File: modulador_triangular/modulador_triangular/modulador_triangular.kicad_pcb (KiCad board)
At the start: 2 copper layers, 50 x 44.5 mm, 12 parts, among them J1 OUT, J2 V1_12, J3 SIN, U1_2 ADTL082, U3 LT1016, U4 ADTL082

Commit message: commit express
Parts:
- added U1: LM7806_TO220, Package_TO_SOT_THT:TO-220-3_Vertical, F.Cu at (157.2, 79.2)
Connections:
- R2 pad 1: Net-(U4-Pin_5) -> Net-(U1-VO)
- U4 pad 5: Net-(U4-Pin_5) -> Net-(U1-VO)

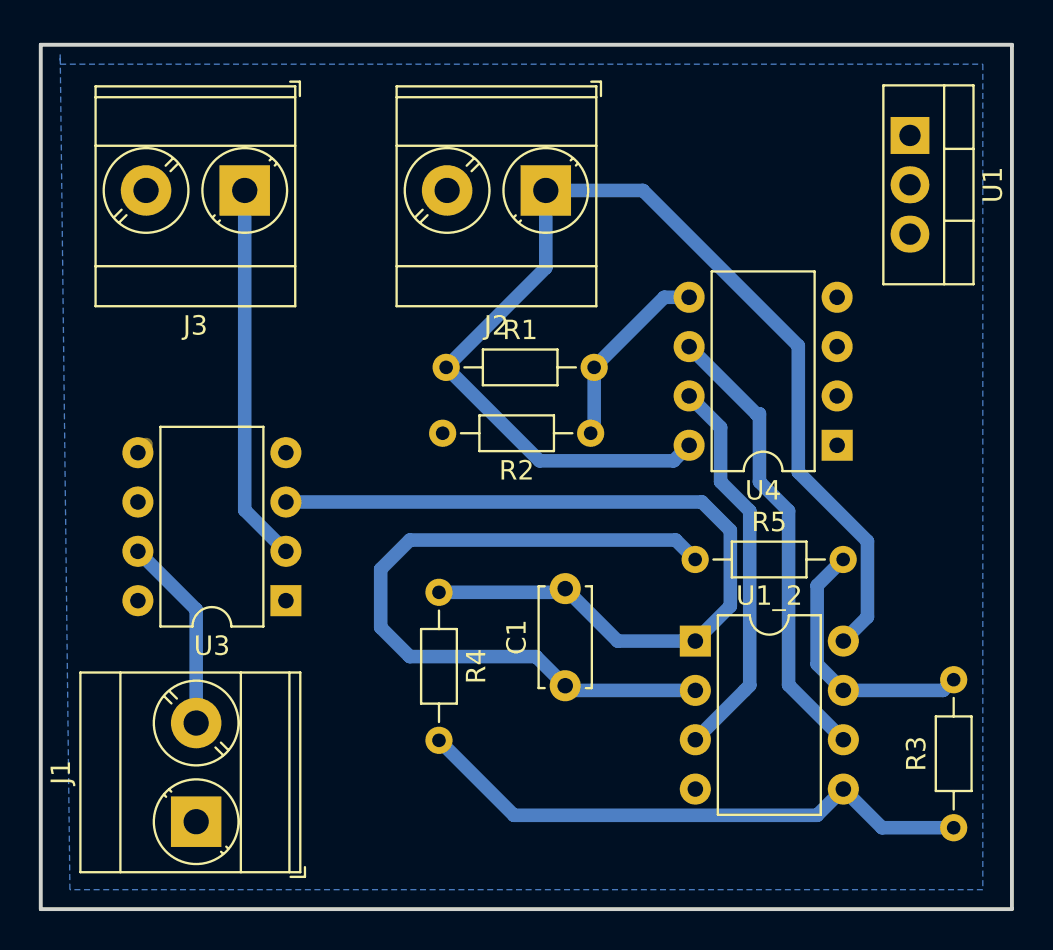
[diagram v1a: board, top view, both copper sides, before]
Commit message: pcb del pwm
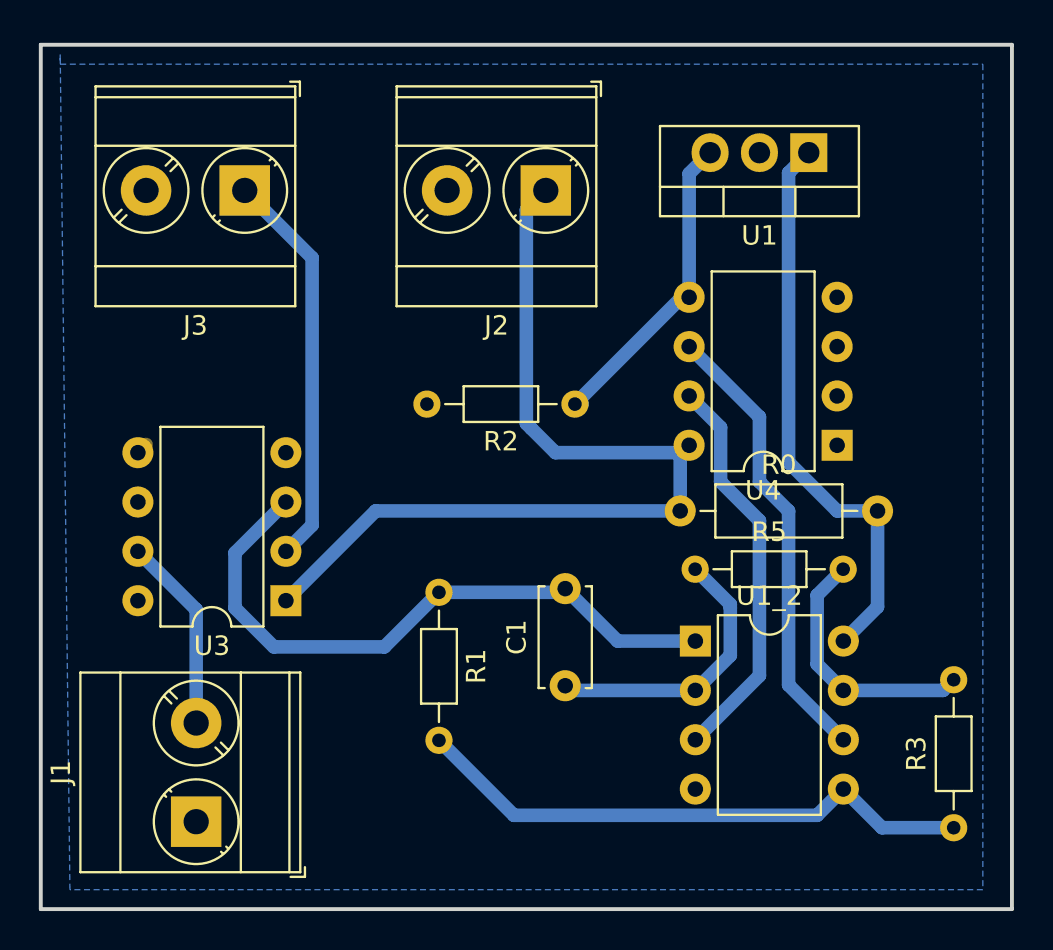
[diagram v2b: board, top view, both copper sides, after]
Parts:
- removed R4: 22K, Resistor_THT:R_Axial_DIN0204_L3.6mm_D1.6mm_P7.62mm_Horizontal
- added R0: 0, Resistor_THT:R_Axial_DIN0207_L6.3mm_D2.5mm_P10.16mm_Horizontal, F.Cu at (145.4, 98.5)
- R1: value 100k -> 22K
- moved R1 11.6 mm to (133.0, 102.7), turned to -90 degrees
- moved U1 5.28 mm to (152.0, 80.1), turned to 180 degrees
- moved R2 1.70 mm to (140.0, 93.0)
- moved R5 0.50 mm to (146.2, 101.5)
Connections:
- R1 pad 1: Vcc -> Vb
- R1 pad 2: Net-(U4-Pin_5) -> Net-(U1_2-Pin_5)
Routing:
- net Net-(U1_2-Pin_2): track 37.8 -> 14.5 mm
- net Vcc: track 59.6 -> 76.8 mm
- net Net-(U1-VO): track 0.00 -> 16.4 mm
- net Vb: track 44.3 -> 33.4 mm
- net Net-(U4-Pin_5): track 9.85 -> 0.00 mm
- net Vr: track 19.5 -> 20.6 mm
- net Va: track 13.8 -> 13.3 mm

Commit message: pcb del pwm
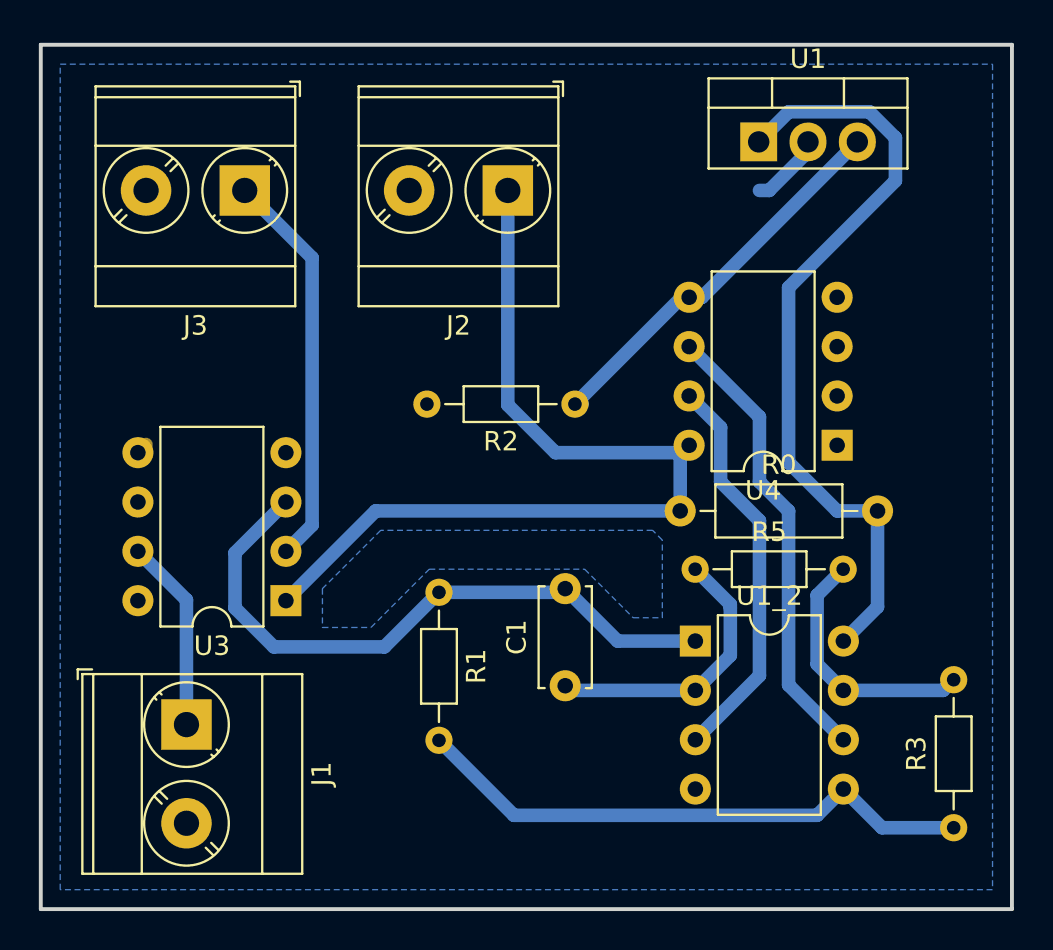
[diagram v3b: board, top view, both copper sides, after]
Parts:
- moved J1 5.02 mm to (120.0, 109.5), turned to -90 degrees
- moved U1 2.64 mm to (149.5, 79.5), turned to 0 degrees
- moved J2 1.96 mm to (136.5, 82.0)
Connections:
- J1 pad 1: GND -> Net-(J1-Pin_1)
- J1 pad 2: Net-(J1-Pin_2) -> GND
- U3 pad 7: Net-(J1-Pin_2) -> Net-(J1-Pin_1)
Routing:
- net Vcc: track 76.8 -> 87.6 mm
- net Net-(J1-Pin_2): track 10.1 -> 0.00 mm
- net Net-(J1-Pin_1): track 0.00 -> 9.96 mm
- net Net-(U1-VO): track 16.4 -> 20.5 mm
- net GND: track 0.59 -> 4.42 mm
- added copper zone on B.Cu, net (none)

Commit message: modificaciones de pcb del pwm
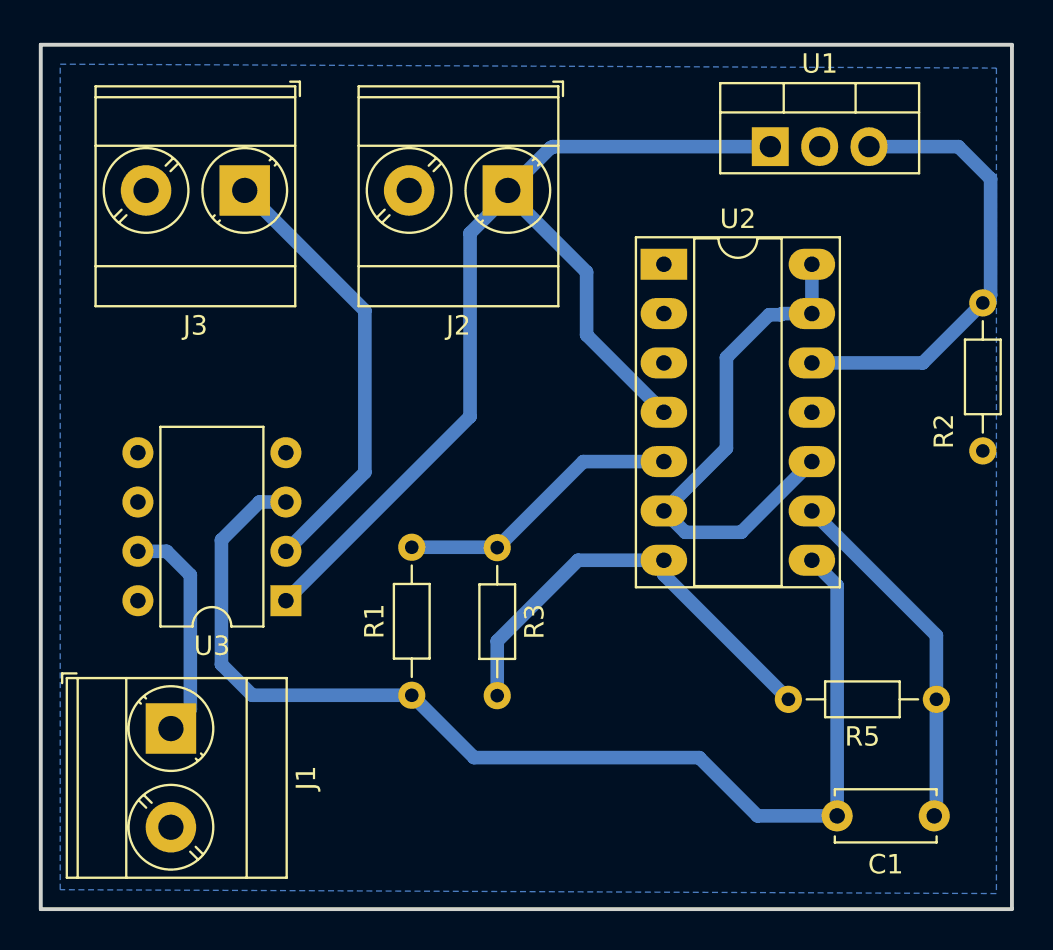
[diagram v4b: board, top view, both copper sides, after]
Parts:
- removed R0: 0, Resistor_THT:R_Axial_DIN0207_L6.3mm_D2.5mm_P10.16mm_Horizontal
- removed U1_2, U4: ADTL082, Package_DIP:DIP-8_W7.62mm
- added U2: TL084, Package_DIP:DIP-14_W7.62mm_Socket_LongPads, F.Cu at (144.6, 85.8)
- moved R3 27.6 mm to (136.0, 100.4), turned to -90 degrees
- moved R2 21.6 mm to (161.0, 87.8), turned to -90 degrees
- moved C1 20.1 mm to (158.5, 114.2), turned to 180 degrees
- moved R5 14.1 mm to (158.6, 108.2), turned to 180 degrees
- moved R1 5.48 mm to (131.6, 108.0), turned to 90 degrees
- moved J1 0.83 mm to (119.2, 109.7)
- moved U1 0.65 mm to (150.1, 79.7)
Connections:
- U3 pad 6: unconnected-(U3-Pin_6-Pad6) -> GND
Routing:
- net Vcc: track 87.6 -> 55.3 mm
- net Vb: track 33.4 -> 59.2 mm
- net Net-(U1_2-Pin_3): track 20.6 -> 0.00 mm
- net Net-(U2B-+): track 29.5 -> 14.8 mm
- net Va: track 13.3 -> 22.9 mm
- net GND: track 4.42 -> 0.00 mm
- net Net-(U2C--): track 14.5 -> 18.4 mm
- net in_-: track 23.5 -> 27.3 mm
- net Net-(U1-VO): track 20.5 -> 23.6 mm
- net Vr: track 20.6 -> 22.8 mm
- net Net-(J1-Pin_1): track 9.96 -> 11.5 mm
- removed copper zone on B.Cu, net (none)

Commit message: modificaciones en la support
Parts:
- removed U2: TL084, Package_DIP:DIP-14_W7.62mm_Socket_LongPads
- removed U3: LT1016, Package_DIP:DIP-8_W7.62mm
- added C2: 0.1u, Capacitor_THT:C_Disc_D5.0mm_W2.5mm_P5.00mm, F.Cu at (156.1, 86.5)
- added C3: 0.33u, Capacitor_THT:C_Disc_D5.0mm_W2.5mm_P5.00mm, F.Cu at (146.1, 84.4)
- added R4: 10k, Resistor_THT:R_Axial_DIN0207_L6.3mm_D2.5mm_P7.62mm_Horizontal, F.Cu at (127.1, 93.2)
- added R6: 1k, Resistor_THT:R_Axial_DIN0207_L6.3mm_D2.5mm_P7.62mm_Horizontal, F.Cu at (130.0, 90.3)
- added U4: TL082, Package_DIP:DIP-8_W7.62mm_LongPads, F.Cu at (151.2, 98.4)
- added U5: LM393, Package_DIP:DIP-8_W7.62mm_LongPads, F.Cu at (138.7, 103.5)
- C1: value 220p -> 470p
- R1: value 22K -> 100K; footprint Resistor_THT:R_Axial_DIN0204_L3.6mm_D1.6mm_P7.62mm_Horizontal -> Resistor_THT:R_Axial_DIN0207_L6.3mm_D2.5mm_P7.62mm_Horizontal
- R2, R5: footprint Resistor_THT:R_Axial_DIN0204_L3.6mm_D1.6mm_P7.62mm_Horizontal -> Resistor_THT:R_Axial_DIN0207_L6.3mm_D2.5mm_P7.62mm_Horizontal
- R3: value 150K -> 390K; footprint Resistor_THT:R_Axial_DIN0204_L3.6mm_D1.6mm_P7.62mm_Horizontal -> Resistor_THT:R_Axial_DIN0207_L6.3mm_D2.5mm_P7.62mm_Horizontal
- moved R1 15.9 mm to (146.9, 112.4)
- moved J2 14.8 mm to (121.8, 81.3)
- moved J3 12.6 mm to (118.5, 93.8), turned to -90 degrees
- moved R3 7.96 mm to (142.7, 96.1)
- moved U1 3.98 mm to (146.3, 78.5)
- moved C1 3.30 mm to (157.7, 111.0), turned to -90 degrees
- moved R2 1.97 mm to (159.6, 86.5), turned to 90 degrees
- moved R5 1.56 mm to (157.6, 107.0)
- moved J1 0.35 mm to (119.4, 109.4)
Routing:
- net Vcc: track 55.3 -> 123.2 mm
- net in_-: track 27.3 -> 58.6 mm
- net Va: track 22.9 -> 37.8 mm
- net Vb: track 59.2 -> 72.5 mm
- net (no net): track 0.00 -> 7.02 mm, vias 0 -> 2
- net Vr: track 22.8 -> 16.7 mm
- net Net-(U1-VO): track 23.6 -> 18.6 mm
- net Net-(J1-Pin_1): track 11.5 -> 15.9 mm
- net Net-(U4A--): track 18.4 -> 14.2 mm
- net Net-(U5A-+): track 14.8 -> 15.4 mm
